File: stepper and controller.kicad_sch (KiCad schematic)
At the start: 30 parts, among them U21 UT6K3, U22 UT6K3, U23 TMC5160-WA, U24 UT6K3, U25 UT6K3

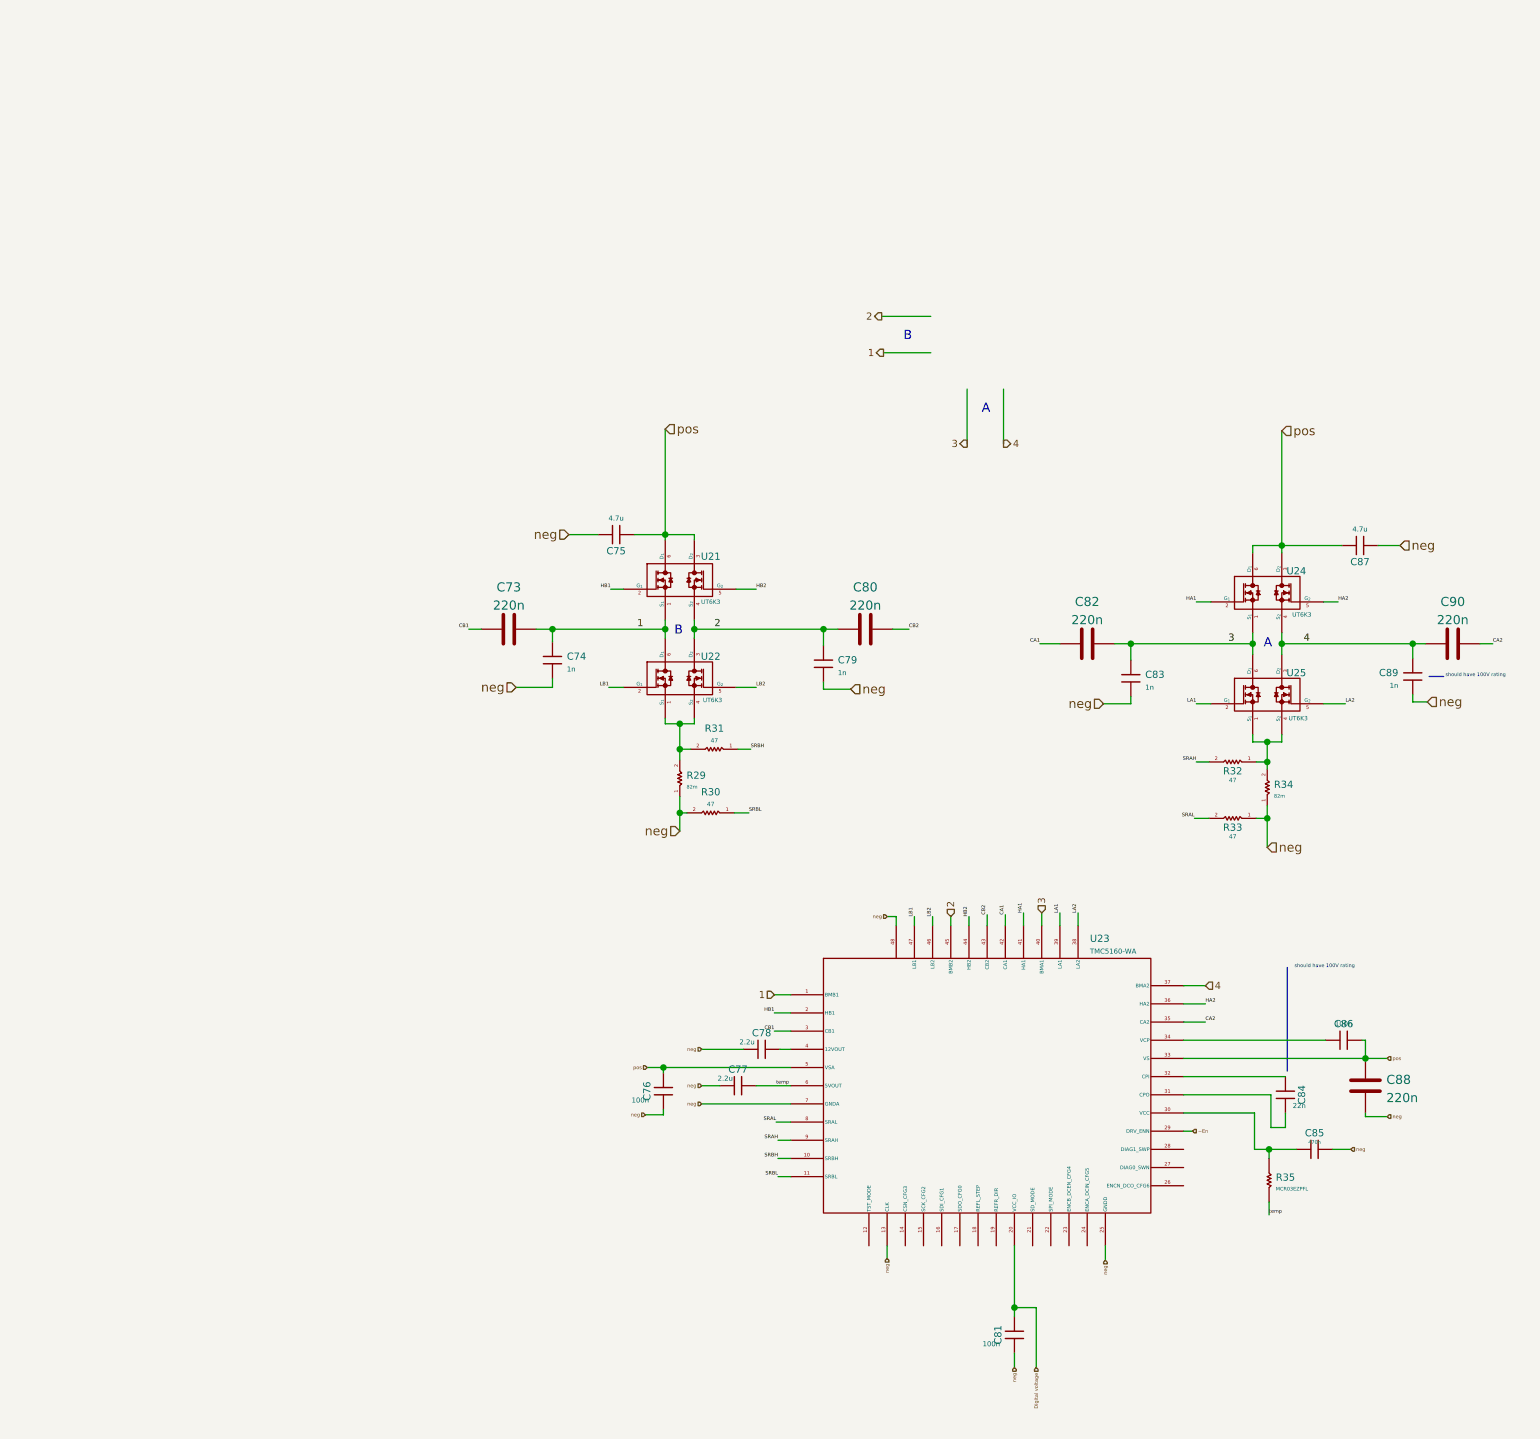
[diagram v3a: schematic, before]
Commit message: base schematic and PCB made
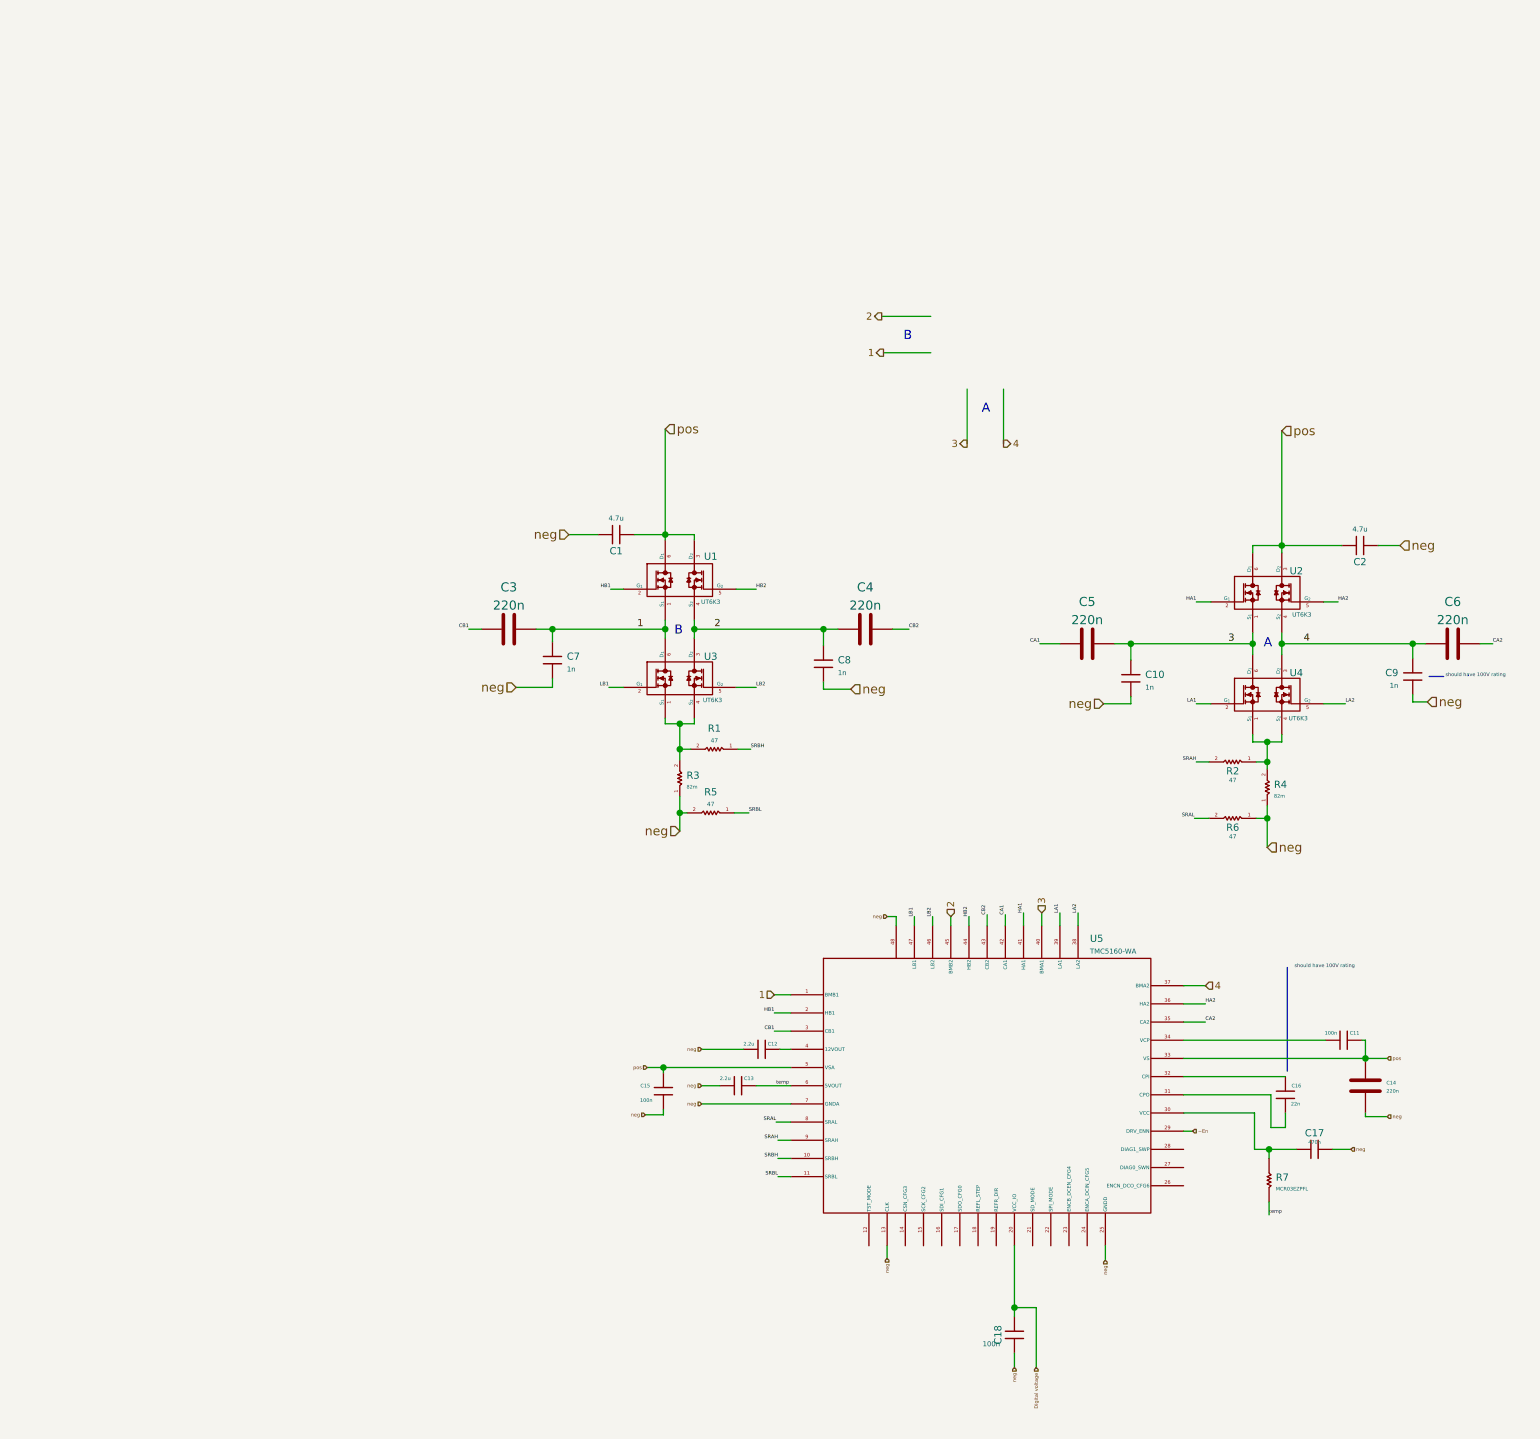
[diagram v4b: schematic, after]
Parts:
- C1: renamed from C75; footprint my_footprints:C0603X105J4RACTU -> Capacitors:C0603X105J4RACTU
- C10: renamed from C83; footprint my_footprints:C0603X105J4RACTU -> Capacitors:C0603X105J4RACTU
- C11: renamed from C86; footprint my_footprints:C0603X105J4RACTU -> Capacitors:C0603X105J4RACTU
- C12: renamed from C78; footprint my_footprints:C0603X105J4RACTU -> Capacitors:C0603X105J4RACTU
- C13: renamed from C77; footprint my_footprints:C0603X105J4RACTU -> Capacitors:C0603X105J4RACTU
- C14: renamed from C88; footprint (none) -> Capacitors:C0603X105J4RACTU
- C15: renamed from C76; footprint my_footprints:C0603X105J4RACTU -> Capacitors:C0603X105J4RACTU
- C16: renamed from C84; footprint my_footprints:C0603X105J4RACTU -> Capacitors:C0603X105J4RACTU
- C17: renamed from C85; footprint my_footprints:C0603X105J4RACTU -> Capacitors:C0603X105J4RACTU
- C18: renamed from C81; footprint my_footprints:C0603X105J4RACTU -> Capacitors:C0603X105J4RACTU
- C2: renamed from C87; footprint my_footprints:C0603X105J4RACTU -> Capacitors:C0603X105J4RACTU
- C3: renamed from C73; footprint (none) -> Capacitors:C0603X105J4RACTU
- C4: renamed from C80; footprint (none) -> Capacitors:C0603X105J4RACTU
- C5: renamed from C82; footprint (none) -> Capacitors:C0603X105J4RACTU
- C6: renamed from C90; footprint (none) -> Capacitors:C0603X105J4RACTU
- C7: renamed from C74; footprint my_footprints:C0603X105J4RACTU -> Capacitors:C0603X105J4RACTU
- C8: renamed from C79; footprint my_footprints:C0603X105J4RACTU -> Capacitors:C0603X105J4RACTU
- C9: renamed from C89; footprint my_footprints:C0603X105J4RACTU -> Capacitors:C0603X105J4RACTU
- R1: renamed from R31; footprint my_footprints:MCR03EZPFX -> Resistors:MCR03EZPFX; symbol resistors:MCR03EZPFX -> Resistors:MCR03EZPFX
- R2: renamed from R32; footprint my_footprints:MCR03EZPFX -> Resistors:MCR03EZPFX; symbol resistors:MCR03EZPFX -> Resistors:MCR03EZPFX
- R3: renamed from R29; footprint my_footprints:GMR50HJBFWR082 -> Resistors:GMR50HJBFWR082; symbol resistors:GMR50HJBFWR082 -> Resistors:GMR50HJBFWR082
- R4: renamed from R34; footprint my_footprints:GMR50HJBFWR082 -> Resistors:GMR50HJBFWR082; symbol resistors:GMR50HJBFWR082 -> Resistors:GMR50HJBFWR082
- R5: renamed from R30; footprint my_footprints:MCR03EZPFX -> Resistors:MCR03EZPFX; symbol resistors:MCR03EZPFX -> Resistors:MCR03EZPFX
- R6: renamed from R33; footprint my_footprints:MCR03EZPFX -> Resistors:MCR03EZPFX; symbol resistors:MCR03EZPFX -> Resistors:MCR03EZPFX
- R7: renamed from R35; footprint my_footprints:MCR03EZPFL -> Resistors:MCR03EZPFL; symbol resistors:MCR03EZPFL -> Resistors:MCR03EZPFL
- U1: renamed from U21; footprint my_footprints:UT6K3TCR -> E-MOSFETs:UT6K3TCR
- U2: renamed from U24; footprint my_footprints:UT6K3TCR -> E-MOSFETs:UT6K3TCR
- U3: renamed from U22; footprint my_footprints:UT6K3TCR -> E-MOSFETs:UT6K3TCR
- U4: renamed from U25; footprint my_footprints:UT6K3TCR -> E-MOSFETs:UT6K3TCR
- U5: renamed from U23; footprint my_footprints:TMC5160-WA -> ICs:TMC5160-WA

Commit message: minor changes
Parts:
- C1, C2: value 4.7u -> (none); footprint Capacitors:C0603X105J4RACTU -> (none)
- C10, C7, C8, C9: value 1n -> (none); footprint Capacitors:C0603X105J4RACTU -> (none)
- C11, C15, C18: value 100n -> (none); footprint Capacitors:C0603X105J4RACTU -> (none)
- C12, C13: value 2.2u -> (none); footprint Capacitors:C0603X105J4RACTU -> (none)
- C14, C3, C4, C5, C6: value 220n -> (none); footprint Capacitors:C0603X105J4RACTU -> (none)
- C16: value 22n -> (none); footprint Capacitors:C0603X105J4RACTU -> (none)
- C17: value 470n -> (none); footprint Capacitors:C0603X105J4RACTU -> (none)
- R1, R2, R5, R6: value 47 -> (none); footprint Resistors:MCR03EZPFX -> (none)
- R3, R4: value 82m -> (none); footprint Resistors:GMR50HJBFWR082 -> (none)
- R7: value MCR03EZPFL -> (none); footprint Resistors:MCR03EZPFL -> (none)
- U1, U2, U3, U4: value UT6K3 -> (none); footprint E-MOSFETs:UT6K3TCR -> (none)
- U5: value TMC5160-WA -> (none); footprint ICs:TMC5160-WA -> (none)
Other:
- company: (none) -> 3D ROBOT
- title: 3D robot project - electronics -> Base circuit - TH
